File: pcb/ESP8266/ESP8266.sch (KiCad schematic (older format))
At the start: 22 parts, among them J1 Conn_02x04, U1 ESP8266EX, U2 W25Q16BVSSIG

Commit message: agregado de comentarios
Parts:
- C1, C2, C3, C4: footprint Capacitor_SMD:C_0402_1005Metric -> Capacitor_SMD:C_0805_2012Metric
- C5: footprint Capacitor_SMD:C_0603_1608Metric -> Capacitor_SMD:C_0805_2012Metric
- D1, D2, R1, R2, R3, R4, R5: footprint Resistor_SMD:R_0402_1005Metric -> Resistor_SMD:R_0805_2012Metric
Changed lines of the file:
@@
 F 0 "R1" H 9045 2796 50  0000 L CNN
 F 1 "12K+/-1%" H 9025 2700 50  0000 L CNN
-F 2 "Resistor_SMD:R_0402_1005Metric" V 8905 2750 50  0001 C CNN
+F 2 "Resistor_SMD:R_0805_2012Metric" V 8905 2750 50  0001 C CNN
 F 3 "~" H 8975 2750 50  0001 C CNN
 	1    8975 2750
@@
 F 0 "R2" V 5425 4025 50  0000 C CNN
 F 1 "200" V 5500 4025 50  0000 C CNN
-F 2 "Resistor_SMD:R_0402_1005Metric" V 5580 4025 50  0001 C CNN
+F 2 "Resistor_SMD:R_0805_2012Metric" V 5580 4025 50  0001 C CNN
 F 3 "~" H 5650 4025 50  0001 C CNN
 	1    5650 4025
@@
 F 0 "C3" H 5065 2946 50  0000 L CNN
 F 1 "0.1uF" H 5065 2855 50  0000 L CNN
-F 2 "Capacitor_SMD:C_0402_1005Metric" H 4988 2750 50  0001 C CNN
+F 2 "Capacitor_SMD:C_0805_2012Metric" H 4988 2750 50  0001 C CNN
 F 3 "~" H 4950 2900 50  0001 C CNN
 	1    4950 2900
@@
 F 0 "C4" V 9525 3500 50  0000 C CNN
 F 1 "5.6pF" V 9625 3500 50  0000 C CNN
-F 2 "Capacitor_SMD:C_0402_1005Metric" H 9413 3350 50  0001 C CNN
+F 2 "Capacitor_SMD:C_0805_2012Metric" H 9413 3350 50  0001 C CNN
 F 3 "~" H 9375 3500 50  0001 C CNN
 	1    9375 3500
@@
 F 0 "C5" H 4590 2946 50  0000 L CNN
 F 1 "10uF" H 4590 2855 50  0000 L CNN
-F 2 "Capacitor_SMD:C_0603_1608Metric" H 4513 2750 50  0001 C CNN
+F 2 "Capacitor_SMD:C_0805_2012Metric" H 4513 2750 50  0001 C CNN
 F 3 "~" H 4475 2900 50  0001 C CNN
 	1    4475 2900
@@
 F 0 "R3" V 5750 2750 50  0000 C CNN
 F 1 "0" V 5825 2775 50  0000 C CNN
-F 2 "Resistor_SMD:R_0402_1005Metric" V 5580 2700 50  0001 C CNN
+F 2 "Resistor_SMD:R_0805_2012Metric" V 5580 2700 50  0001 C CNN
 F 3 "~" H 5650 2700 50  0001 C CNN
 	1    5650 2700
@@
 F 0 "R4" H 2680 3204 50  0000 R CNN
 F 1 "4K7" H 2680 3295 50  0000 R CNN
-F 2 "Resistor_SMD:R_0402_1005Metric" V 2680 3250 50  0001 C CNN
+F 2 "Resistor_SMD:R_0805_2012Metric" V 2680 3250 50  0001 C CNN
 F 3 "~" H 2750 3250 50  0001 C CNN
 	1    2750 3250
@@
 F 0 "R5" H 3400 2850 50  0000 R CNN
 F 1 "2K2" H 3450 2950 50  0000 R CNN
-F 2 "Resistor_SMD:R_0402_1005Metric" V 3155 2900 50  0001 C CNN
+F 2 "Resistor_SMD:R_0805_2012Metric" V 3155 2900 50  0001 C CNN
 F 3 "~" H 3225 2900 50  0001 C CNN
 	1    3225 2900
@@
 F 0 "D1" V 2789 2757 50  0000 R CNN
 F 1 "RED LED" V 2698 2757 50  0000 R CNN
-F 2 "Resistor_SMD:R_0402_1005Metric" H 2750 2875 50  0001 C CNN
+F 2 "Resistor_SMD:R_0805_2012Metric" H 2750 2875 50  0001 C CNN
 F 3 "~" H 2750 2875 50  0001 C CNN
 	1    2750 2875
@@
 F 0 "D2" V 3300 3450 50  0000 R CNN
 F 1 "BLUE LED" V 3200 3700 50  0000 R CNN
-F 2 "Resistor_SMD:R_0402_1005Metric" H 3225 3275 50  0001 C CNN
+F 2 "Resistor_SMD:R_0805_2012Metric" H 3225 3275 50  0001 C CNN
 F 3 "~" H 3225 3275 50  0001 C CNN
 	1    3225 3275
@@
 F 0 "C1" H 5075 6200 50  0000 L CNN
 F 1 "CAP NP" H 4900 6100 50  0000 L CNN
-F 2 "Capacitor_SMD:C_0402_1005Metric" H 5338 6000 50  0001 C CNN
+F 2 "Capacitor_SMD:C_0805_2012Metric" H 5338 6000 50  0001 C CNN
 F 3 "~" H 5300 6150 50  0001 C CNN
 	1    5300 6150
@@
 F 0 "C2" H 4515 6196 50  0000 L CNN
 F 1 "CAP NP" H 4515 6105 50  0000 L CNN
-F 2 "Capacitor_SMD:C_0402_1005Metric" H 4438 6000 50  0001 C CNN
+F 2 "Capacitor_SMD:C_0805_2012Metric" H 4438 6000 50  0001 C CNN
 F 3 "~" H 4400 6150 50  0001 C CNN
 	1    4400 6150
@@
 	5800 2700 6075 2700
 $Comp
-L power:+3.3V #PWR?
+L power:+3.3V #PWR0104
 U 1 1 5F8AA151
 P 4825 5550
-F 0 "#PWR?" H 4825 5400 50  0001 C CNN
+F 0 "#PWR0104" H 4825 5400 50  0001 C CNN
 F 1 "+3.3V" H 4840 5723 50  0000 C CNN
 F 2 "" H 4825 5550 50  0001 C CNN

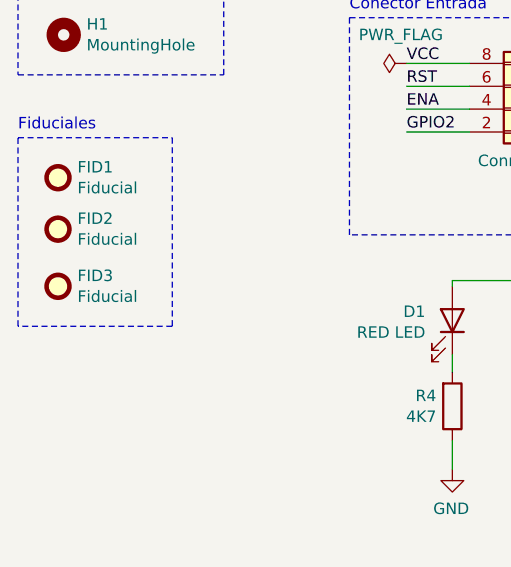
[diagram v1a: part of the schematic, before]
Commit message: agregados componentes digikey
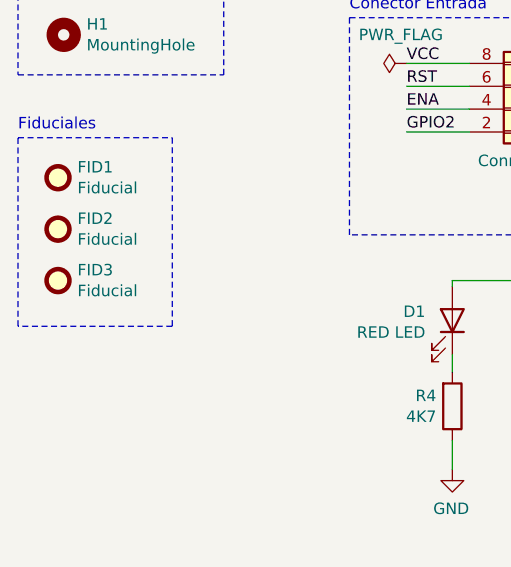
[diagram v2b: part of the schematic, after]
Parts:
- C1, C2, C3, C4, C5: Digikey (none) -> https://www.digikey.com/en/products/detail/C0805C104K5RACTU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; Digikey Nr (none) -> 399-1170-2-ND
- D1: Digikey (none) -> https://www.digikey.com/en/products/detail/osram-opto-semic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; Digikey Nr (none) -> 475-1410-2-ND
- D2: Digikey  (none) -> https://www.digikey.com/en/products/detail/osram-opto-semic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; Digikey Nr (none) -> 475-1410-2-ND
- J1: Digikey (none) -> https://www.digikey.com/catalog/en/partgroup/0-100-2-54mm-p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
- L1, L2: Digikey (none) -> https://www.digikey.com/en/products/detail/kemet/L0805C100M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; Digikey Nr (none) -> 399-9583-2-ND
- R1, R2, R3, R4, R5: Digikey (none) -> https://www.digikey.com/en/products/detail/yageo/RC0805JR-0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; Digikey Nr (none) -> 311-390ARTR-ND
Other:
- moved on the sheet: FID3
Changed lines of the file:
@@
 Comp "CESE11 - Federico Pacher"
 Comment1 "Revisor Hanes Sciarrone"
-Comment2 ""
+Comment2 "Licencia Libre"
 Comment3 ""
 Comment4 ""
@@
 F 2 "Resistor_SMD:R_0805_2012Metric" V 8905 2750 50  0001 C CNN
 F 3 "~" H 8975 2750 50  0001 C CNN
+F 4 "https://www.digikey.com/en/products/detail/yageo/RC0805JR-07390RL/731266" H 8975 2750 50  0001 C CNN "Digikey"
+F 5 "311-390ARTR-ND" H 8975 2750 50  0001 C CNN "Digikey Nr"
 	1    8975 2750
 	-1   0    0    -1
@@
 F 2 "Resistor_SMD:R_0805_2012Metric" V 5580 4025 50  0001 C CNN
 F 3 "~" H 5650 4025 50  0001 C CNN
+F 4 "https://www.digikey.com/en/products/detail/yageo/RC0805JR-07390RL/731266" V 5650 4025 50  0001 C CNN "Digikey"
+F 5 "311-390ARTR-ND" V 5650 4025 50  0001 C CNN "Digikey Nr"
 	1    5650 4025
 	0    -1   1    0
@@
 F 2 "Capacitor_SMD:C_0805_2012Metric" H 4988 2750 50  0001 C CNN
 F 3 "~" H 4950 2900 50  0001 C CNN
+F 4 "https://www.digikey.com/en/products/detail/C0805C104K5RACTU/399-1170-1-ND/411445" H 4950 2900 50  0001 C CNN "Digikey"
+F 5 "399-1170-2-ND" H 4950 2900 50  0001 C CNN "Digikey Nr"
 	1    4950 2900
 	-1   0    0    -1
@@
 F 2 "Capacitor_SMD:C_0805_2012Metric" H 9413 3350 50  0001 C CNN
 F 3 "~" H 9375 3500 50  0001 C CNN
+F 4 "https://www.digikey.com/en/products/detail/C0805C104K5RACTU/399-1170-1-ND/411445" V 9375 3500 50  0001 C CNN "Digikey"
+F 5 "399-1170-2-ND" V 9375 3500 50  0001 C CNN "Digikey Nr"
 	1    9375 3500
 	0    -1   1    0
@@
 F 2 "Capacitor_SMD:C_0805_2012Metric" H 4513 2750 50  0001 C CNN
 F 3 "~" H 4475 2900 50  0001 C CNN
+F 4 "https://www.digikey.com/en/products/detail/C0805C104K5RACTU/399-1170-1-ND/411445" H 4475 2900 50  0001 C CNN "Digikey"
+F 5 "399-1170-2-ND" H 4475 2900 50  0001 C CNN "Digikey Nr"
 	1    4475 2900
 	-1   0    0    -1
@@
 F 2 "Resistor_SMD:R_0805_2012Metric" V 5580 2700 50  0001 C CNN
 F 3 "~" H 5650 2700 50  0001 C CNN
+F 4 "https://www.digikey.com/en/products/detail/yageo/RC0805JR-07390RL/731266" V 5650 2700 50  0001 C CNN "Digikey"
+F 5 "311-390ARTR-ND" V 5650 2700 50  0001 C CNN "Digikey Nr"
 	1    5650 2700
 	0    -1   1    0
@@
 F 2 "Resistor_SMD:R_0805_2012Metric" V 2680 3250 50  0001 C CNN
 F 3 "~" H 2750 3250 50  0001 C CNN
+F 4 "https://www.digikey.com/en/products/detail/yageo/RC0805JR-07390RL/731266" H 2750 3250 50  0001 C CNN "Digikey"
+F 5 "311-390ARTR-ND" H 2750 3250 50  0001 C CNN "Digikey Nr"
 	1    2750 3250
 	1    0    0    1
@@
 F 2 "Resistor_SMD:R_0805_2012Metric" V 3155 2900 50  0001 C CNN
 F 3 "~" H 3225 2900 50  0001 C CNN
+F 4 "https://www.digikey.com/en/products/detail/yageo/RC0805JR-07390RL/731266" H 3225 2900 50  0001 C CNN "Digikey"
+F 5 "311-390ARTR-ND" H 3225 2900 50  0001 C CNN "Digikey Nr"
 	1    3225 2900
 	1    0    0    1
@@
 F 2 "Resistor_SMD:R_0805_2012Metric" H 2750 2875 50  0001 C CNN
 F 3 "~" H 2750 2875 50  0001 C CNN
+F 4 "https://www.digikey.com/en/products/detail/osram-opto-semiconductors-inc/LG-R971-KN-1/1227925" V 2750 2875 50  0001 C CNN "Digikey"
+F 5 "475-1410-2-ND" V 2750 2875 50  0001 C CNN "Digikey Nr"
 	1    2750 2875
 	0    1    -1   0
@@
 F 2 "Resistor_SMD:R_0805_2012Metric" H 3225 3275 50  0001 C CNN
 F 3 "~" H 3225 3275 50  0001 C CNN
+F 4 "https://www.digikey.com/en/products/detail/osram-opto-semiconductors-inc/LG-R971-KN-1/1227925" V 3225 3275 50  0001 C CNN "Digikey "
+F 5 "475-1410-2-ND" V 3225 3275 50  0001 C CNN "Digikey Nr"
 	1    3225 3275
 	0    1    -1   0
@@
 F 2 "Connector_PinHeader_2.54mm:PinHeader_2x04_P2.54mm_Vertical" H 3125 1950 50  0001 C CNN
 F 3 "~" H 3125 1950 50  0001 C CNN
+F 4 "https://www.digikey.com/catalog/en/partgroup/0-100-2-54mm-pitch-connector-headers/24994" H 3125 1950 50  0001 C CNN "Digikey"
 	1    3125 1950
 	-1   0    0    1
@@
 F 2 "Inductor_SMD:L_0805_2012Metric" H 9675 3650 50  0001 C CNN
 F 3 "~" H 9675 3650 50  0001 C CNN
+F 4 "https://www.digikey.com/en/products/detail/kemet/L0805C100MDWLT/3674101" H 9675 3650 50  0001 C CNN "Digikey"
+F 5 "399-9583-2-ND" H 9675 3650 50  0001 C CNN "Digikey Nr"
 	1    9675 3650
 	1    0    0    1
@@
 F 2 "Inductor_SMD:L_0805_2012Metric" H 9075 3650 50  0001 C CNN
 F 3 "~" H 9075 3650 50  0001 C CNN
+F 4 "https://www.digikey.com/en/products/detail/kemet/L0805C100MDWLT/3674101" H 9075 3650 50  0001 C CNN "Digikey"
+F 5 "399-9583-2-ND" H 9075 3650 50  0001 C CNN "Digikey Nr"
 	1    9075 3650
 	1    0    0    1
@@
 L Mechanical:Fiducial FID3
 U 1 1 5F8B4929
-P 1025 2725
-F 0 "FID3" H 1110 2771 50  0000 L CNN
-F 1 "Fiducial" H 1110 2680 50  0000 L CNN
-F 2 "Fiducial:Fiducial_1mm_Mask2mm" H 1025 2725 50  0001 C CNN
-F 3 "~" H 1025 2725 50  0001 C CNN
-	1    1025 2725
+P 1025 2700
+F 0 "FID3" H 1110 2746 50  0000 L CNN
+F 1 "Fiducial" H 1110 2655 50  0000 L CNN
+F 2 "Fiducial:Fiducial_1mm_Mask2mm" H 1025 2700 50  0001 C CNN
+F 3 "~" H 1025 2700 50  0001 C CNN
+	1    1025 2700
 	1    0    0    -1
 $EndComp
@@
 F 2 "Capacitor_SMD:C_0805_2012Metric" H 5338 6000 50  0001 C CNN
 F 3 "~" H 5300 6150 50  0001 C CNN
+F 4 "https://www.digikey.com/en/products/detail/C0805C104K5RACTU/399-1170-1-ND/411445" H 5300 6150 50  0001 C CNN "Digikey"
+F 5 "399-1170-2-ND" H 5300 6150 50  0001 C CNN "Digikey Nr"
 	1    5300 6150
 	-1   0    0    -1
@@
 F 2 "Capacitor_SMD:C_0805_2012Metric" H 4438 6000 50  0001 C CNN
 F 3 "~" H 4400 6150 50  0001 C CNN
+F 4 "https://www.digikey.com/en/products/detail/C0805C104K5RACTU/399-1170-1-ND/411445" H 4400 6150 50  0001 C CNN "Digikey"
+F 5 "399-1170-2-ND" H 4400 6150 50  0001 C CNN "Digikey Nr"
 	1    4400 6150
 	-1   0    0    -1

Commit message: agregado de logos y e informacion para fabricacion
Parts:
- added LOGO1: Logo_Open_Hardware_Small, Symbol:KiCad-Logo2_5mm_Copper, symbol Graphic:Logo_Open_Hardware_Small
- added LOGO2: Logo_Open_Hardware_Small, Symbol:OSHW-Logo2_7.3x6mm_Copper, symbol Graphic:Logo_Open_Hardware_Small
- renumbered XTAL1 to Y1
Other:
- note added: "Logos"
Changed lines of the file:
@@
 encoding utf-8
 Sheet 1 1
-Title "Replica mejorada modulo Wifi ESP-01S"
-Date "2020-09-11"
-Rev "v1.0"
-Comp "CESE11 - Federico Pacher"
-Comment1 "Revisor Hanes Sciarrone"
-Comment2 "Licencia Libre"
-Comment3 ""
+Title "Wifi Module ESP-01S"
+Date "2020-11-05"
+Rev "Rev: 1.0"
+Comp "Microelect"
+Comment1 "Author: Federico Pacher"
+Comment2 "Reviewer: Hanes Sciarrones"
+Comment3 "CERN Open Hardware Licence Version 2 - Permissive"
 Comment4 ""
 $EndDescr
@@
 	6025 6600 3950 6600
 $Comp
-L Oscillator:XO53 XTAL1
+L Oscillator:XO53 Y1
 U 1 1 5F5BFCC2
 P 4825 5925
-F 0 "XTAL1" H 4500 5650 50  0000 L CNN
+F 0 "Y1" H 4550 5650 50  0000 L CNN
 F 1 "40MHz" H 4475 5550 50  0000 L CNN
 F 2 "Oscillator:Oscillator_SMD_EuroQuartz_XO32-4Pin_3.2x2.5mm" H 5525 5575 50  0001 C CNN
@@
 Wire Notes Line
 	3950 5325 3950 6600
+$Comp
+L Graphic:Logo_Open_Hardware_Small LOGO1
+U 1 1 5FA45A8D
+P 1175 3550
+F 0 "LOGO1" H 1175 3825 50  0001 C CNN
+F 1 "Logo_Open_Hardware_Small" H 1175 3325 50  0001 C CNN
+F 2 "Symbol:KiCad-Logo2_5mm_Copper" H 1175 3550 50  0001 C CNN
+F 3 "~" H 1175 3550 50  0001 C CNN
+	1    1175 3550
+	1    0    0    -1
+$EndComp
+$Comp
+L Graphic:Logo_Open_Hardware_Small LOGO2
+U 1 1 5FA46376
+P 1175 4150
+F 0 "LOGO2" H 1175 4425 50  0001 C CNN
+F 1 "Logo_Open_Hardware_Small" H 1175 3925 50  0001 C CNN
+F 2 "Symbol:OSHW-Logo2_7.3x6mm_Copper" H 1175 4150 50  0001 C CNN
+F 3 "~" H 1175 4150 50  0001 C CNN
+	1    1175 4150
+	1    0    0    -1
+$EndComp
+Text Notes 850  3175 0    50   ~ 0
+Logos
+Wire Notes Line
+	850  3200 1525 3200
+Wire Notes Line
+	1525 3200 1525 4400
+Wire Notes Line
+	1525 4400 850  4400
+Wire Notes Line
+	850  4400 850  3200
 $EndSCHEMATC
